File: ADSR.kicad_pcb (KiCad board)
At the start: 2 copper layers, 9.9 x 110.1 mm, 44 parts, among them J1 Gate, J2 Out, Q1 BC847, Q2 BC847, Q3 BC847, Q4 MMBT3904, U1 NE555, U2 LM358

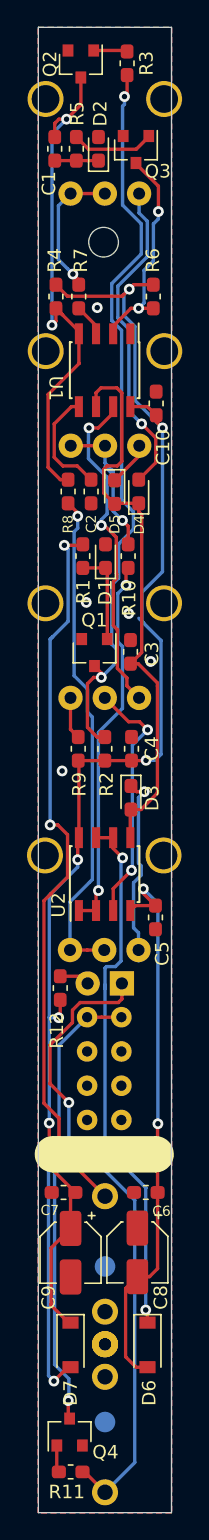
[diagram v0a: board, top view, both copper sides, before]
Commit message: v.0.3 - Fixed the pot and C3 values. Changed transistors to MBT3904
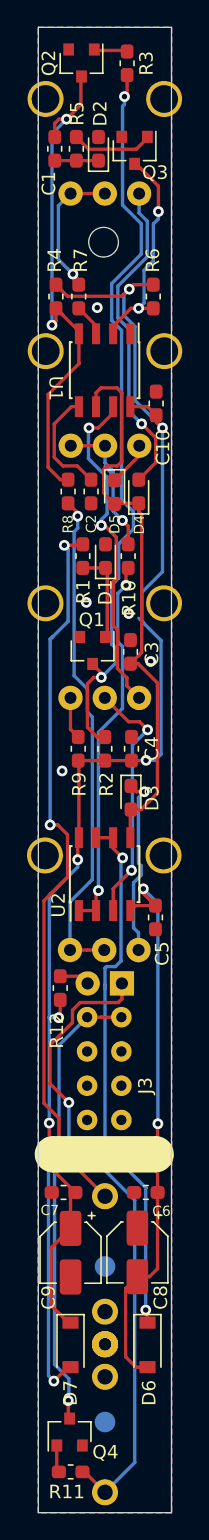
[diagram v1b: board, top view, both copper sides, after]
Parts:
- C3: value 4u7 -> 2.2u
- Q1, Q2, Q3: value BC847 -> MMBT3904
- RV1: value A1M -> B1M
- RV2, RV4: value A1M -> B500k
- moved Q1 0.21 mm to (38.0, 66.2)
- moved Q3 0.12 mm to (41.1, 29.1)
- moved Q2 0.09 mm to (37.2, 22.6)
- renumbered ~ to J3
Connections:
- J3 pad 1: Net-(D6-Pad1) -> Net-(J3-Pad1)
- J3 pad 3: GND -> Net-(J3-Pad3)
- J3 pad 5: GND -> Net-(J3-Pad5)
- J3 pad 7: GND -> Net-(J3-Pad7)
- J3 pad 9: Net-(D7-Pad2) -> Net-(J3-Pad9)
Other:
- board text added: "+"
- board text added: "-"
- board text added: "ADSR v0.3"
- board text added: "Fastest Envelope in the West"
- board text added: "by René Schmitz"
- board text removed: "ADSR v0.2"
